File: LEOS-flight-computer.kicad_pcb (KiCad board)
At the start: 2 copper layers, 100 x 100 mm, 29 parts, among them J1 MicroFit_1x4, J2 MicroFit_1x4, J3 GPIO, J4 I2C Breakout, J5 SPI Breakout, U1 MCP2562FD, U2 MCP2518FD, U3 SAM-M8Q, Y1 40 MHz

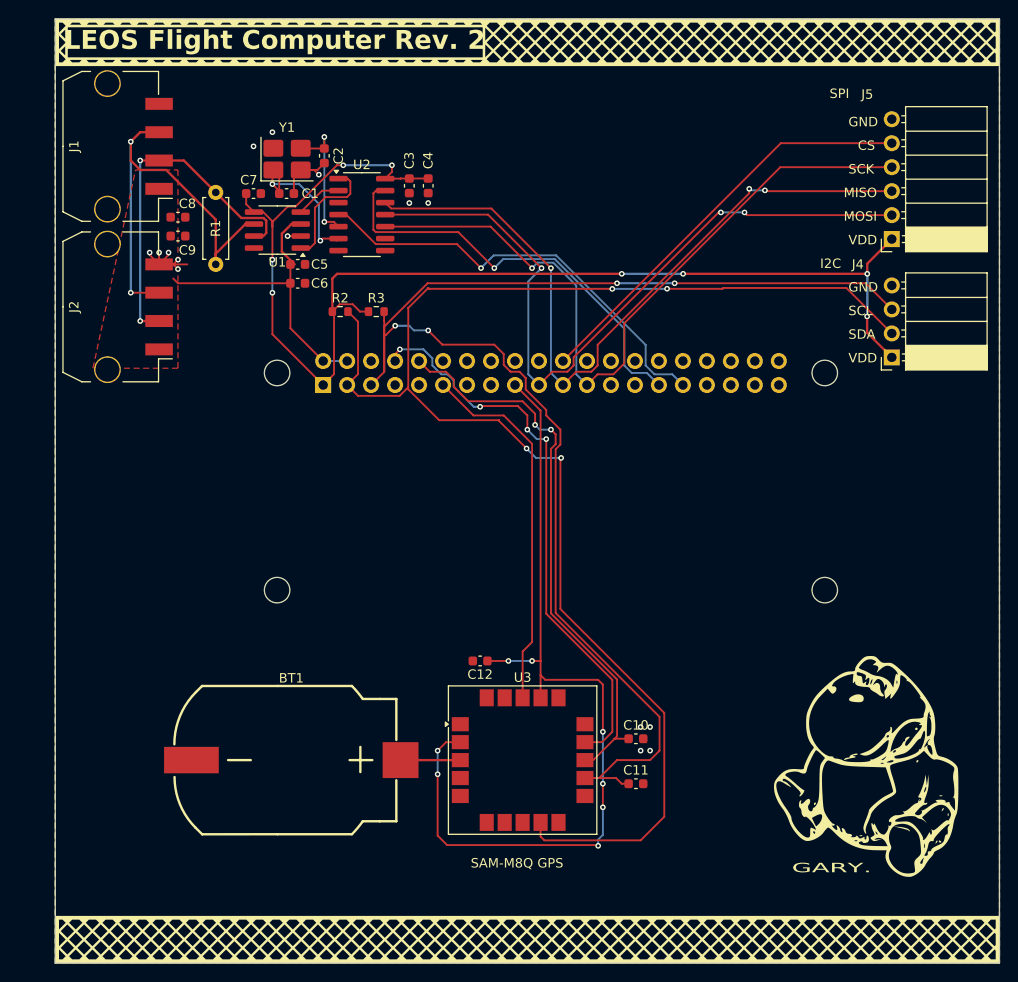
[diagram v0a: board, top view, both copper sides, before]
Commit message: v2.1 with redesigned board, connectors, and improved access to RPi
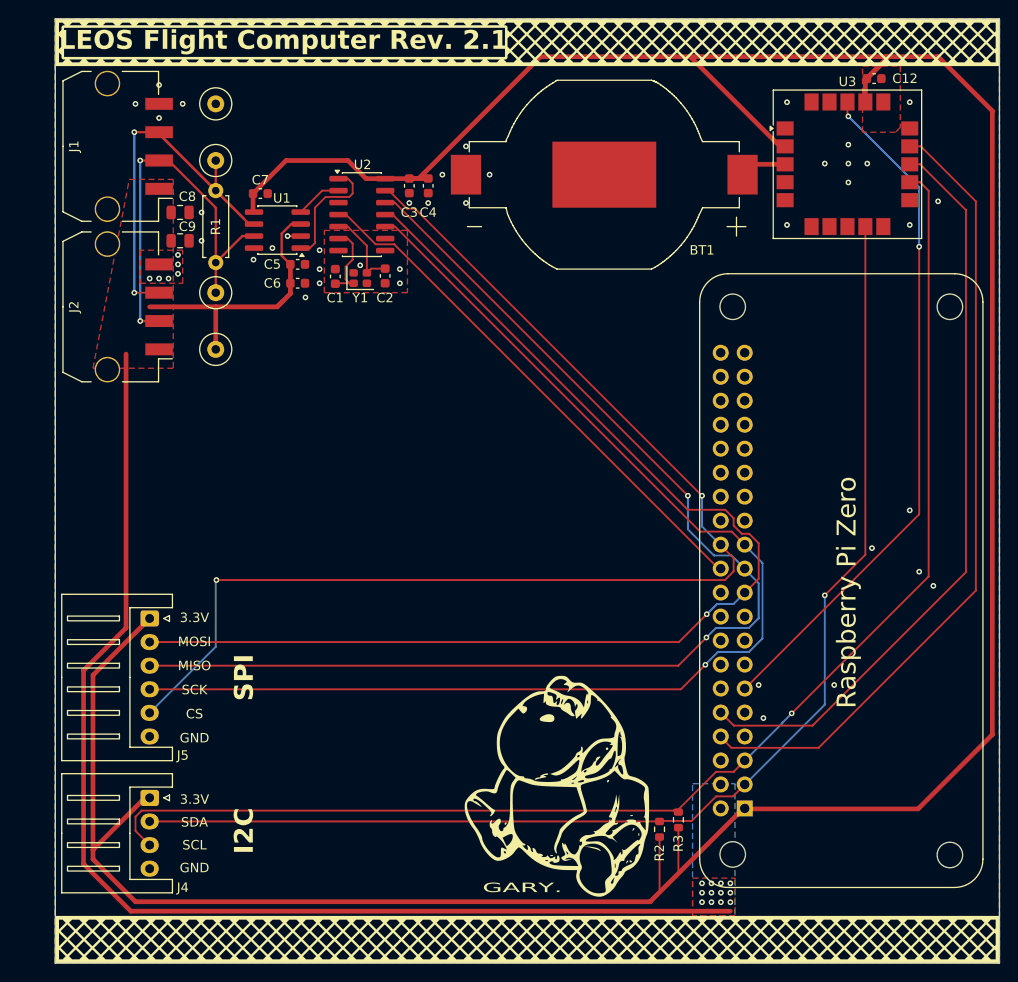
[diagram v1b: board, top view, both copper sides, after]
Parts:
- removed C10, C11: 34pF, Capacitor_SMD:C_0603_1608Metric
- removed MH1, MH2, MH3, MH4: MountingHole_2.7mm_M2.5, MountingHole:MountingHole_2.7mm_M2.5
- added H1: MountingHole, MountingHole:MountingHole_2.7mm_M2.5, F.Cu at (171.8, 138.5)
- added H2: MountingHole, MountingHole:MountingHole_2.7mm_M2.5, F.Cu at (171.8, 80.5)
- added H3: MountingHole, MountingHole:MountingHole_2.7mm_M2.5, F.Cu at (194.8, 138.6)
- added H4: MountingHole, MountingHole:MountingHole_2.7mm_M2.5, F.Cu at (194.8, 80.5)
- added TP1: CAN-H Test Point, TestPoint:TestPoint_Loop_D2.60mm_Drill0.9mm_Beaded, F.Cu at (117.0, 79.0)
- added TP2: CAN-L Test Point, TestPoint:TestPoint_Loop_D2.60mm_Drill0.9mm_Beaded, F.Cu at (117.0, 65.0)
- added TP3: 5V Test Point, TestPoint:TestPoint_Loop_D2.60mm_Drill0.9mm_Beaded, F.Cu at (117.0, 85.0)
- added TP4: GND Test Point, TestPoint:TestPoint_Loop_D2.60mm_Drill0.9mm_Beaded, F.Cu at (117.0, 59.0)
- BT1: value Battery_Cell -> GPS Battery Backup; footprint CustomFootprints:BatteryHolder_SMD_MYOUNG_BS-08-B2AA010-R -> LEOS:BAT_BU2032SM-JJ-GTR
- C1, C2: value 12pF -> 10p
- C12: value 0.1 uF -> 0.1u
- C3, C5, C7: value 0.1uF -> 0.1u
- C4, C6: value 1uF -> 1u
- C8: value 47uF -> 22u; footprint Capacitor_SMD:C_0603_1608Metric -> Capacitor_SMD:C_0805_2012Metric
- C9: value 0.1uF -> 22u; footprint Capacitor_SMD:C_0603_1608Metric -> Capacitor_SMD:C_0805_2012Metric
- J1, J2: footprint Connector_Molex:Molex_Micro-Fit_3.0_43650-0410_1x04-1MP_P3.00mm_Horizontal_PnP -> LEOS:Molex_MicroFit3.0_43650-0410_1x04_Horizontal
- J4: value I2C Breakout -> JST XH; footprint Connector_PinSocket_2.54mm:PinSocket_1x04_P2.54mm_Horizontal -> Connector_JST:JST_XH_S4B-XH-A_1x04_P2.50mm_Horizontal
- J5: value SPI Breakout -> JST XH; footprint Connector_PinSocket_2.54mm:PinSocket_1x06_P2.54mm_Horizontal -> Connector_JST:JST_XH_S6B-XH-A_1x06_P2.50mm_Horizontal
- R1: value 120R -> 120
- U3: footprint RF_GPS:ublox_SAM-M8Q -> LEOS:ublox_SAM-M8Q
- Y1: footprint Crystal:Crystal_SMD_3225-4Pin_3.2x2.5mm_HandSoldering -> Crystal:Crystal_SMD_2016-4Pin_2.0x1.6mm
- moved J4 91.4 mm to (110.0, 132.5), turned to -90 degrees
- moved J5 88.3 mm to (110.0, 113.5), turned to -90 degrees
- moved C12 74.5 mm to (186.7, 56.3), turned to 0 degrees
- moved U3 71.9 mm to (183.9, 65.4)
- moved BT1 70.1 mm to (158.2, 66.5), turned to 180 degrees
- moved R2 64.4 mm to (164.0, 135.8), turned to 90 degrees
- moved J3 63.3 mm to (173.0, 133.6), turned to 0 degrees
- moved R3 62.6 mm to (166.0, 134.8), turned to 90 degrees
- moved Y1 14.8 mm to (132.3, 77.5)
- moved C2 14.3 mm to (134.9, 77.2)
- moved C1 10.2 mm to (129.7, 77.3), turned to -90 degrees
- moved R1 7.81 mm to (117.0, 68.2), turned to -90 degrees
- moved C7 0.72 mm to (121.7, 68.5)
- moved C8 0.55 mm to (113.2, 70.5)
- moved C9 0.55 mm to (113.2, 73.5)
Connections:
- net /CAN+ renamed /CANbus/CAN+
- net /CAN- renamed /CANbus/CAN-
- net /OSC2 renamed /CANbus/OSC2
- net /RXCAN renamed Net-(U1-RXD)
- net /TXCAN renamed Net-(U1-TXD)
- net GPIO10/SPI0.MOSI renamed /GPIO10/SPI0.MOSI
- net GPIO11/SPI0.SCLK renamed /GPIO11/SPI0.SCK
- net GPIO14/TXD0 renamed /GPIO14/TXD0
- net GPIO15/RXD0 renamed /GPIO15/RXD0
- net GPIO9/SPI0.MISO renamed /GPIO9/SPI0.MISO
- C1 pad 1: /OSC1 -> GND
- C1 pad 2: GND -> /CANbus/OSC1
- J3 pad 22: GPIO25 -> /GPIO25
- J3 pad 24: GPIO8/SPI0.CE0 -> /GPIO8/SPI0.CE0
- J5 pad 5: GPIO25 -> /GPIO8/SPI0.CE0
- U2 pad 13: GPIO5 -> /GPIO8/SPI0.CE0
- U2 pad 4: GPIO6 -> /GPIO25
- U2 pad 6: /OSC1 -> /CANbus/OSC1
- Y1 pad 1: /OSC1 -> /CANbus/OSC1
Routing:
- net /GPIO8/SPI0.CE0: track 0.00 -> 128.1 mm, vias 0 -> 2
- net +5V: track 33.1 -> 155.9 mm, vias 0 -> 12
- net VDD: track 227.4 -> 331.3 mm, vias 16 -> 0
- net /GPIO25: track 0.00 -> 55.3 mm
- net /GPIO11/SPI0.SCK: track 78.6 -> 129.8 mm
- net /GPIO9/SPI0.MISO: track 78.4 -> 128.6 mm, vias 3 -> 2
- net /GPIO10/SPI0.MOSI: track 77.9 -> 124.7 mm, vias 3 -> 1
- net GPIO6: track 46.3 -> 0.00 mm, vias 1 -> 0
- net GPIO5: track 45.4 -> 0.00 mm, vias 1 -> 0
- net GPIO25: track 44.4 -> 0.00 mm
- net GPIO17: track 39.3 -> 73.0 mm, vias 0 -> 2
- net GPIO2/SDA1: track 156.4 -> 129.0 mm, vias 4 -> 1
- net /GPIO14/TXD0: track 59.9 -> 85.1 mm, vias 4 -> 0
- net /GPIO15/RXD0: track 59.8 -> 79.6 mm, vias 2 -> 0
- net GND: track 19.6 -> 1.39 mm, vias 15 -> 45
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- added copper zone on B.Cu, net +5V
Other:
- board text added: "02/17/2026"
- board text added: "3.3V"
- board text added: "5V"
- board text added: "CAN-H"
- board text added: "CAN-L"
- board text added: "LEOS Flight Computer Rev. 2.1"
- board text added: "Raspberry Pi Zero"
- board text removed: "Extend PCB edge 0.5mm if using SMT header"
- board text removed: "LEOS Flight Computer Rev. 2"
- board text removed: "SAM-M8Q GPS"
- board text removed: "VDD"
